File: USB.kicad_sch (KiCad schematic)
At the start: 12 parts, among them J4 USB_C_16P, J5 USB_A

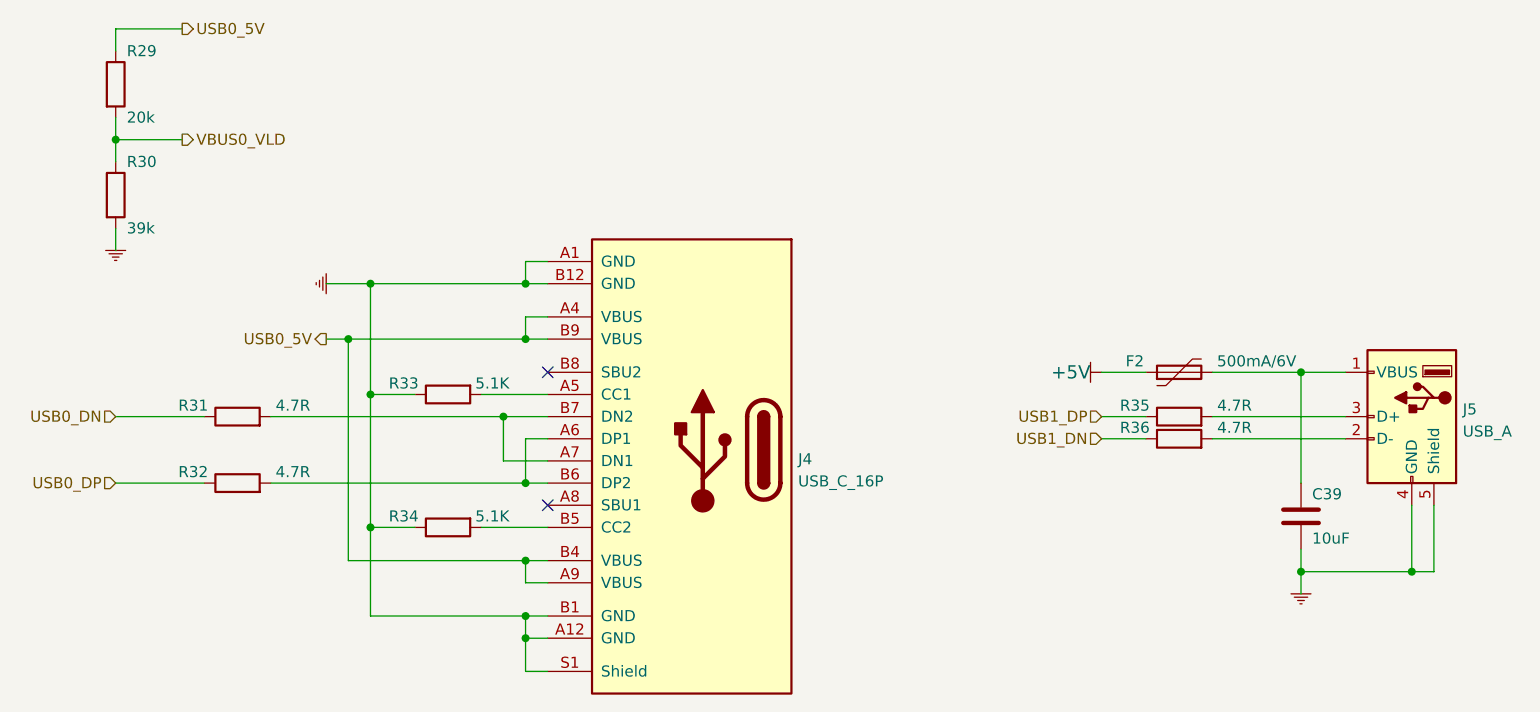
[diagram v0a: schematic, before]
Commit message: update schematic and footprints
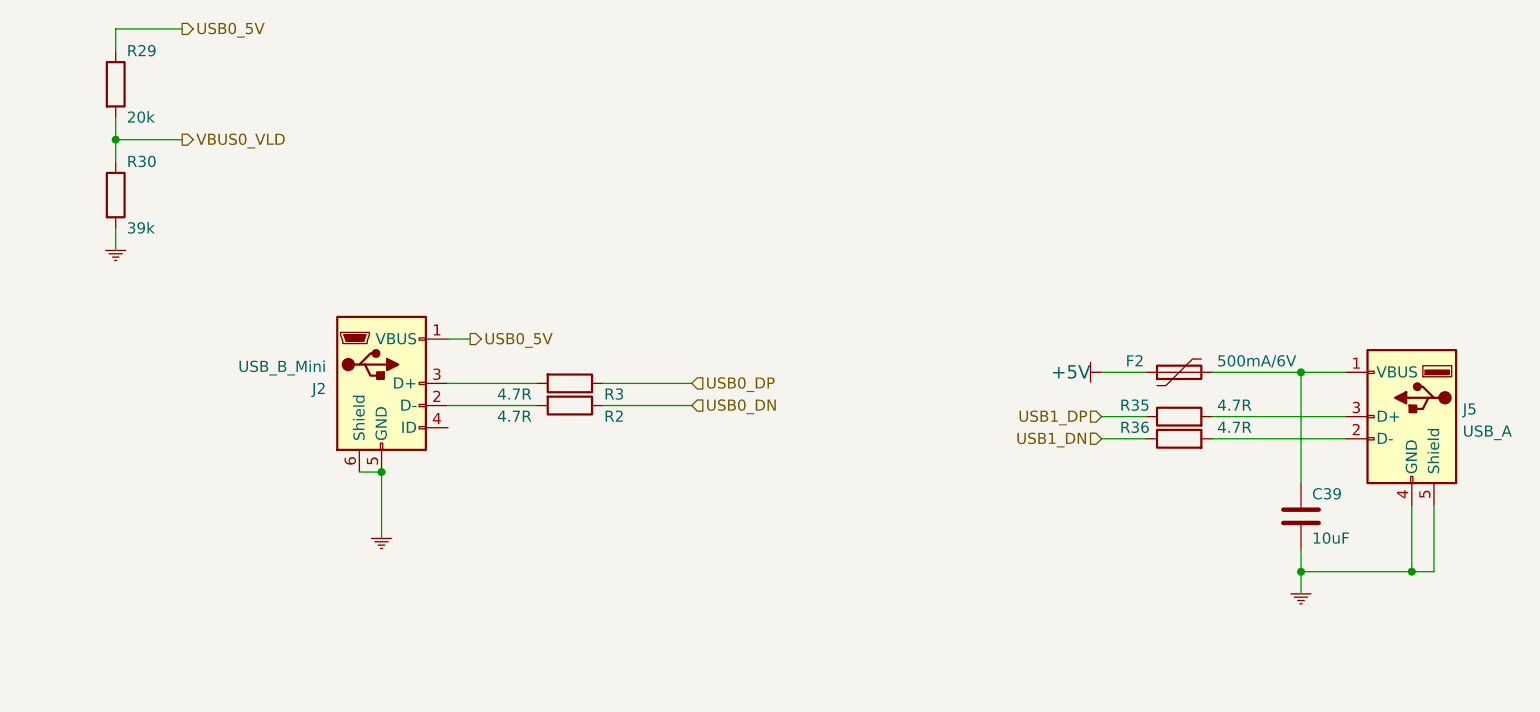
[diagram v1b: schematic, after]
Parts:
- removed J4: USB_C_16P, 0_ungrouped:USB_C_16P_4Foot8.64mm, symbol 0_ungrouped:USB_C_16P
- removed R31, R32: 4.7R, Resistor_SMD:R_0603_1608Metric, symbol Device:R
- removed R33, R34: 5.1K, Resistor_SMD:R_0603_1608Metric, symbol Device:R
- added J2: USB_B_Mini, digikey-footprints:USB_Mini_B_Female_690-005-299-043, symbol Connector:USB_B_Mini
- added R2, R3: 4.7R, Resistor_SMD:R_0805_2012Metric_Pad1.20x1.40mm_HandSolder, symbol Device:R
- C39: footprint Capacitor_SMD:C_0805_2012Metric -> Capacitor_SMD:C_0805_2012Metric_Pad1.18x1.45mm_HandSolder
- J5: footprint 0_ungrouped:USB_A_90Deg_THT_Horizontal -> digikey-footprints:USB_A_Female_UE27AC54100
- R29, R30, R35, R36: footprint Resistor_SMD:R_0603_1608Metric -> Resistor_SMD:R_0805_2012Metric_Pad1.20x1.40mm_HandSolder
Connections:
- net GND: now also J2.5 (GND), J2.6 (Shield)
- net USB0_5V: now also J2.1 (VBUS)
- net USB0_DN: now also R2.1
- net USB0_DP: now also R3.1
- new net: J2.3 (D+), R3.2
- new net: J2.2 (D-), R2.2
- no-connect marks 2 -> 0
